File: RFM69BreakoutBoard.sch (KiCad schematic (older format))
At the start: 22 parts, among them P1 BB Holes, P10 TST, P11 TST, P12 TST, P13 TST, P2 TST, P3 TST, P4 TST, P5 TST, P6 TST, P7 TST, P8 TST, P9 TST, U1 MCP1703, U2 74HCT123, U3 RFM69HW

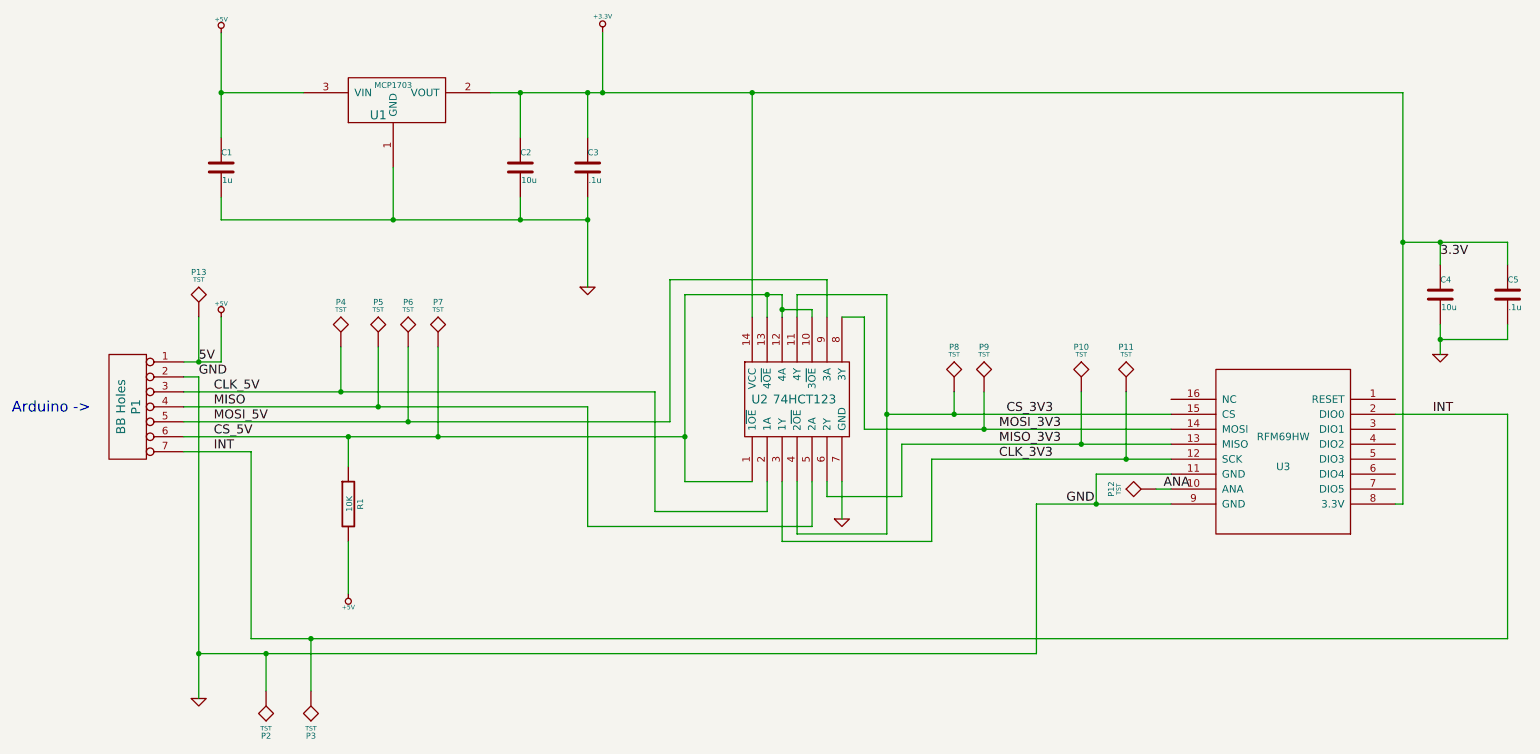
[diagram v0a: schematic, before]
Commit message: 2nd pass at PCB layout
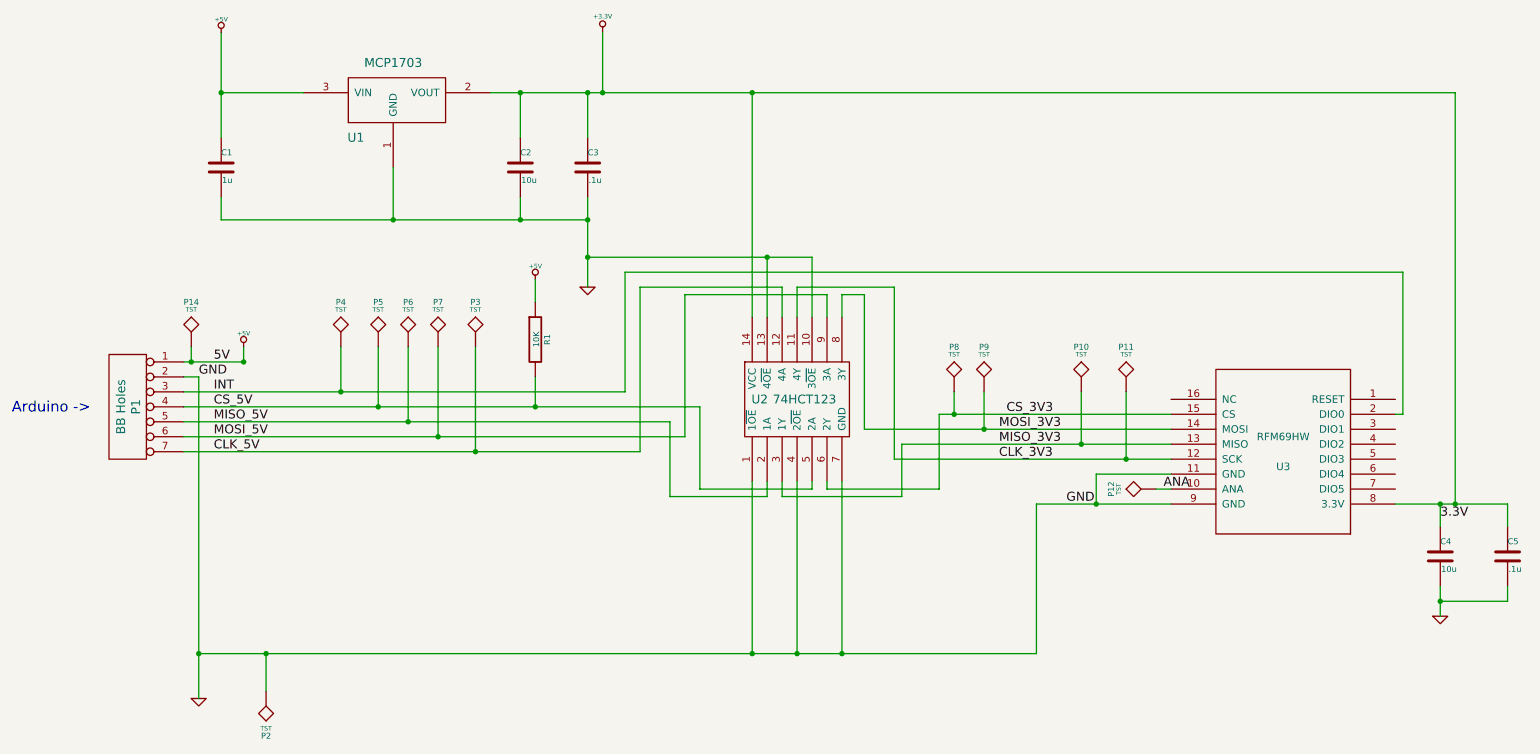
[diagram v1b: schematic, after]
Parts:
- removed P13: TST, ~, symbol TST
- added P14: TST, ~, symbol TST
- U1: Distributor Part Number MCP1703T-3302E/CBCT-ND -> (none); Distributor Part Number Link http://www.digikey.com/product-detail/en/MCP1703T-3302E%2FC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 -> (none); MFG Name Microchip Technology -> (none); MFG Part Number MCP1703T-3302E/CB -> (none)
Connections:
- net MISO is gone; now on net CS_5V: P1.4 (P4), P5.1, U2.5 (2A)
- net +5V: now also R1.1, P14.1; no longer R1.2
- net CLK_3V3: now also U2.11 (4Y); no longer U2.3 (1Y)
- net CLK_5V: now also P1.7 (P7), P3.1, U2.12 (4A); no longer P1.3 (P3), P4.1, U2.2 (1A)
- net CS_3V3: now also U2.6 (2Y); no longer U2.11 (4Y), U2.4 (2~OE)
- net CS_5V: now also R1.2; no longer P1.6 (P6), P7.1, R1.1, U2.1 (1~OE), U2.10 (3~OE), U2.12 (4A), U2.13 (4~OE)
- net GND: now also U2.1 (1~OE), U2.10 (3~OE), U2.13 (4~OE), U2.4 (2~OE)
- net INT: now also P1.3 (P3), P4.1; no longer P1.7 (P7), P3.1
- net MISO_3V3: now also U2.3 (1Y); no longer U2.6 (2Y)
- net MOSI_5V: now also P1.6 (P6), P7.1; no longer P1.5 (P5), P6.1
- new net MISO_5V: P1.5 (P5), P6.1, U2.2 (1A)
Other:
- moved on the sheet: C4, C5, R1

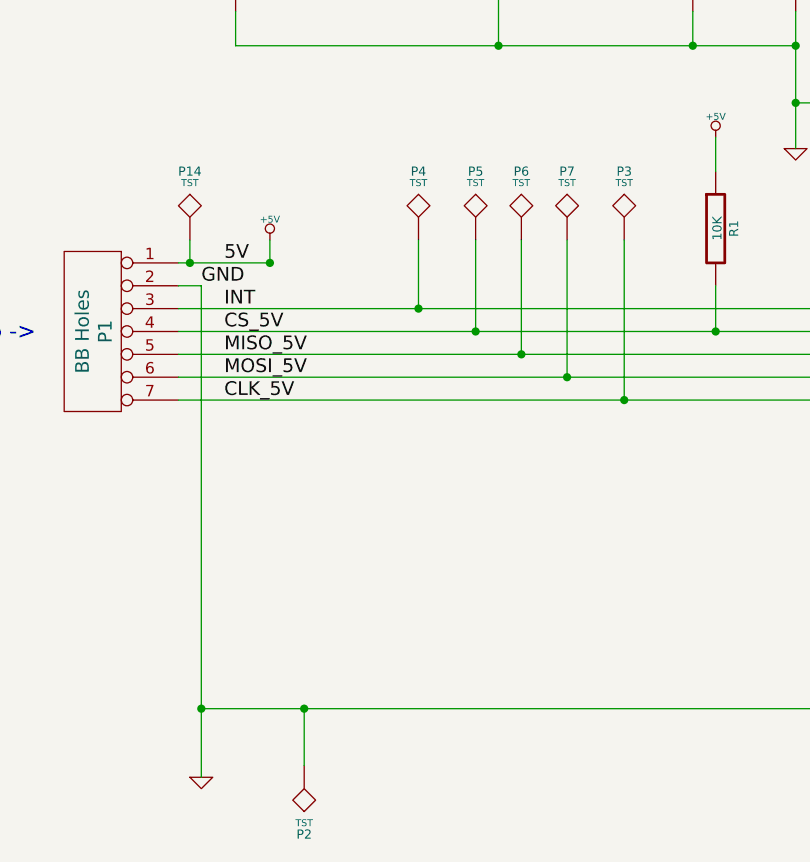
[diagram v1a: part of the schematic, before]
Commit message: removed test points at connector
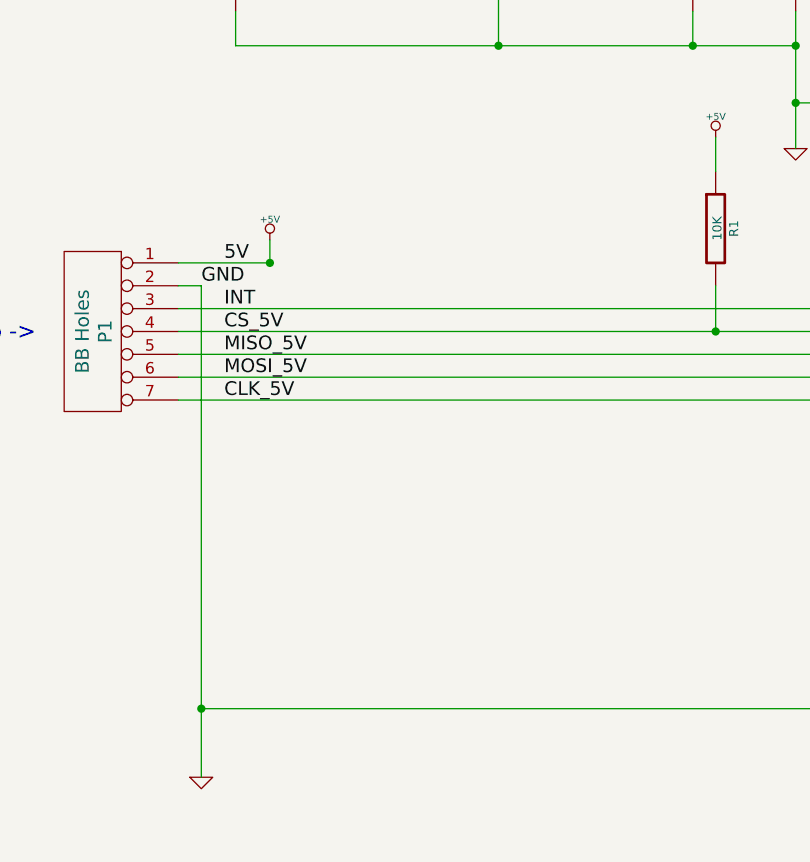
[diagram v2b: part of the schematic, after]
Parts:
- removed P14, P2, P3, P4, P5, P6, P7: TST, ~, symbol TST
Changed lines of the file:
@@
 Sheet 1 1
 Title ""
-Date "12 mar 2014"
+Date "14 mar 2014"
 Rev ""
 Comp ""
@@
 $EndComp
 $Comp
-L +5V #PWR06
-U 1 1 531316EA
-P 2100 4000
-F 0 "#PWR06" H 2100 4090 20  0001 C CNN
-F 1 "+5V" H 2100 4090 30  0000 C CNN
-F 2 "" H 2100 4000 60  0000 C CNN
-F 3 "" H 2100 4000 60  0000 C CNN
-	1    2100 4000
-	-1   0    0    -1
-$EndComp
-$Comp
 L +3.3V #PWR07
 U 1 1 5313177E
@@
 Text Label 10100 5150 0    60   ~ 0
 3.3V
-$Comp
-L TST P4
-U 1 1 5314E601
-P 2750 4000
-F 0 "P4" H 2750 4300 40  0000 C CNN
-F 1 "TST" H 2750 4250 30  0000 C CNN
-F 2 "~" H 2750 4000 60  0000 C CNN
-F 3 "~" H 2750 4000 60  0000 C CNN
-	1    2750 4000
-	1    0    0    -1
-$EndComp
-$Comp
-L TST P5
-U 1 1 5314E60E
-P 3000 4000
-F 0 "P5" H 3000 4300 40  0000 C CNN
-F 1 "TST" H 3000 4250 30  0000 C CNN
-F 2 "~" H 3000 4000 60  0000 C CNN
-F 3 "~" H 3000 4000 60  0000 C CNN
-	1    3000 4000
-	1    0    0    -1
-$EndComp
-$Comp
-L TST P6
-U 1 1 5314E614
-P 3200 4000
-F 0 "P6" H 3200 4300 40  0000 C CNN
-F 1 "TST" H 3200 4250 30  0000 C CNN
-F 2 "~" H 3200 4000 60  0000 C CNN
-F 3 "~" H 3200 4000 60  0000 C CNN
-	1    3200 4000
-	1    0    0    -1
-$EndComp
-$Comp
-L TST P7
-U 1 1 5314E61A
-P 3400 4000
-F 0 "P7" H 3400 4300 40  0000 C CNN
-F 1 "TST" H 3400 4250 30  0000 C CNN
-F 2 "~" H 3400 4000 60  0000 C CNN
-F 3 "~" H 3400 4000 60  0000 C CNN
-	1    3400 4000
-	1    0    0    -1
-$EndComp
-$Comp
-L TST P2
-U 1 1 5314EAED
-P 2250 6300
-F 0 "P2" H 2250 6600 40  0000 C CNN
-F 1 "TST" H 2250 6550 30  0000 C CNN
-F 2 "~" H 2250 6300 60  0000 C CNN
-F 3 "~" H 2250 6300 60  0000 C CNN
-	1    2250 6300
-	-1   0    0    1
-$EndComp
 $Comp
 L TST P10
@@
 	1    0    0    -1
 $EndComp
-$Comp
-L TST P14
-U 1 1 531E2B17
-P 1750 4000
-F 0 "P14" H 1750 4300 40  0000 C CNN
-F 1 "TST" H 1750 4250 30  0000 C CNN
-F 2 "~" H 1750 4000 60  0000 C CNN
-F 3 "~" H 1750 4000 60  0000 C CNN
-	1    1750 4000
-	-1   0    0    -1
-$EndComp
 Wire Wire Line
 	1950 2300 2500 2300
@@
 	10100 5050 10100 5200
 Wire Wire Line
-	2750 4300 2750 4000
-Wire Wire Line
-	3000 4400 3000 4000
-Wire Wire Line
-	2250 6300 2250 6050
-Connection ~ 2250 6050
-Wire Wire Line
 	5500 3800 5500 2300
 Connection ~ 5500 2300
@@
 	6250 4550 8300 4550
 Connection ~ 7050 4550
-Wire Wire Line
-	3400 4000 3400 4600
-Connection ~ 3400 4600
 Wire Wire Line
 	9800 5050 10550 5050
@@
 Connection ~ 6100 6050
 Wire Wire Line
-	2100 4100 2100 4000
-Wire Wire Line
-	1750 4000 1750 4100
-Wire Wire Line
 	1700 4100 2100 4100
 Connection ~ 2100 4100
@@
 	9850 4450 9850 3500
 Wire Wire Line
-	3200 4500 3200 4000
-Wire Wire Line
 	1700 4500 4950 4500
-Connection ~ 3200 4500
 Wire Wire Line
 	1700 4400 5150 4400
-Connection ~ 3000 4400
 Wire Wire Line
 	6750 4450 8300 4450
@@
 	6850 4300 6850 4450
 Connection ~ 6850 4450
-Connection ~ 1750 4100
 Wire Wire Line
 	6500 4650 6500 5000
@@
 Wire Wire Line
 	4650 3500 9850 3500
-Connection ~ 2750 4300
 Wire Wire Line
 	5150 4400 5150 4950
@@
 	4050 4200 4050 4400
 Connection ~ 4050 4400
-$Comp
-L TST P3
-U 1 1 5320C19F
-P 3650 4000
-F 0 "P3" H 3650 4300 40  0000 C CNN
-F 1 "TST" H 3650 4250 30  0000 C CNN
-F 2 "~" H 3650 4000 60  0000 C CNN
-F 3 "~" H 3650 4000 60  0000 C CNN
-	1    3650 4000
-	1    0    0    -1
-$EndComp
-Wire Wire Line
-	3650 4000 3650 4700
-Connection ~ 3650 4700
+Wire Wire Line
+	2100 4100 2100 4000
+$Comp
+L +5V #PWR06
+U 1 1 531316EA
+P 2100 4000
+F 0 "#PWR06" H 2100 4090 20  0001 C CNN
+F 1 "+5V" H 2100 4090 30  0000 C CNN
+F 2 "" H 2100 4000 60  0000 C CNN
+F 3 "" H 2100 4000 60  0000 C CNN
+	1    2100 4000
+	-1   0    0    -1
+$EndComp
 $EndSCHEMATC
